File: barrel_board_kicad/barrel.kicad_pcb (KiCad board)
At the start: 2 copper layers, 29 parts, among them J1 220V, J2 12V, J3 probe/prog, J4 valve, J5 Bypass, J6 reset, K1 DIPxx-1Cxx-51x, Q1 Q_PMOS_GSD, Q2 Q_NMOS_GSD, Q3 Q_PMOS_GSD, U1 LM2576S-5, U2 ATtiny13A-SSU

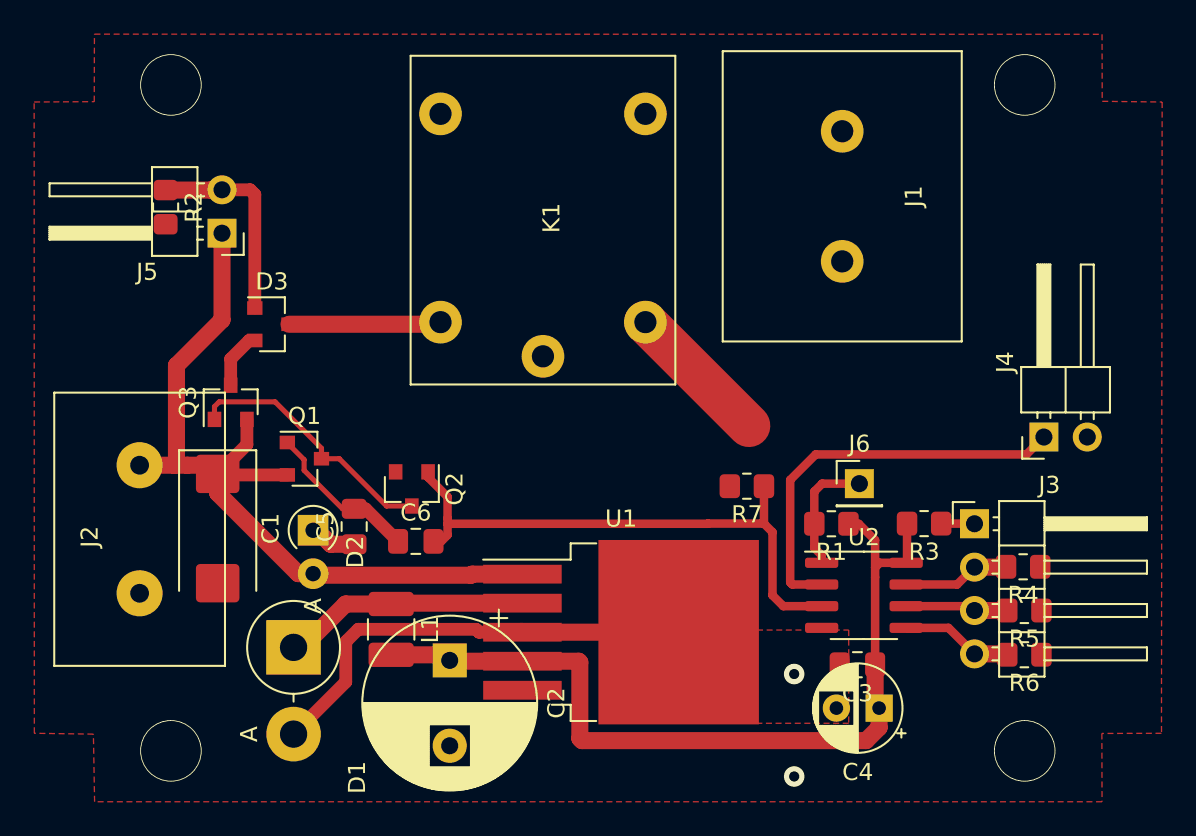
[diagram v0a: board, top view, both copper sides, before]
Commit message: Optimize the scheme
Remove redundant transistors
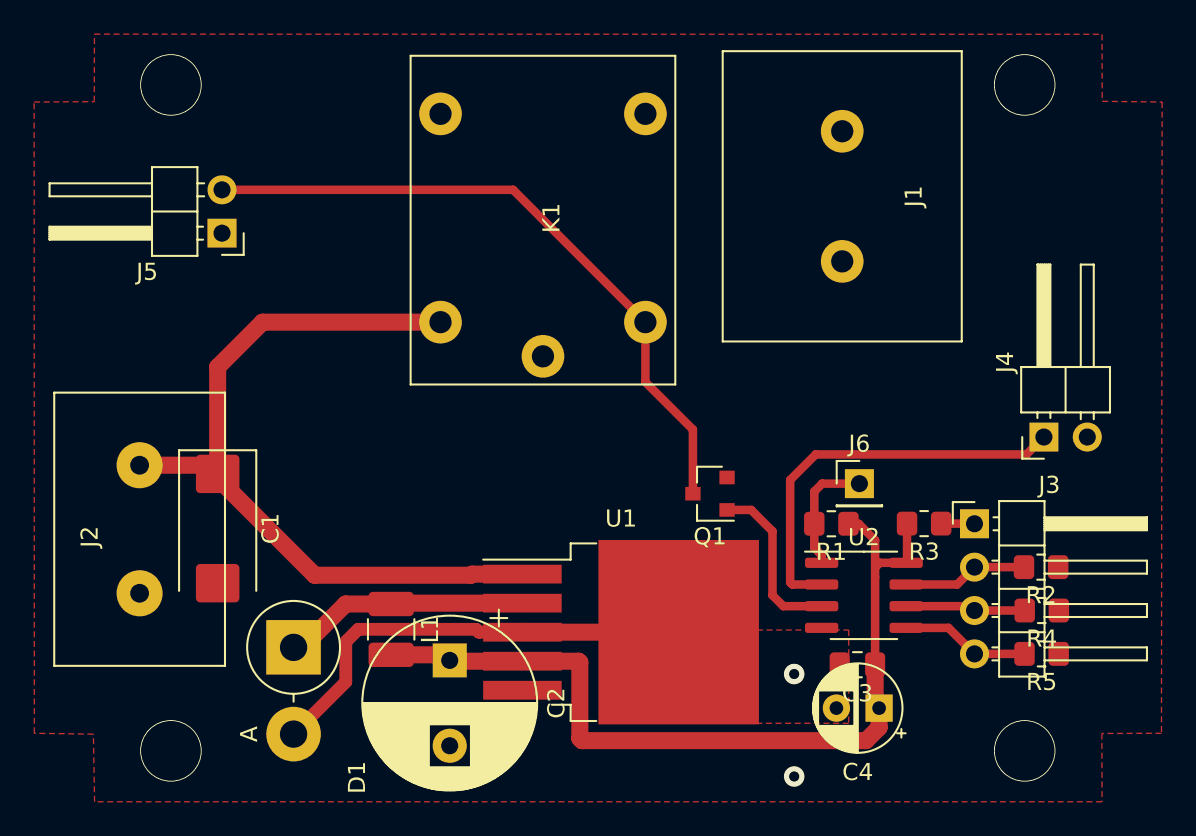
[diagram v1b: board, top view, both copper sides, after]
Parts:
- removed C5: 100nF, Capacitor_SMD:C_0805_2012Metric_Pad1.18x1.45mm_HandSolder
- removed C6: 68nF, Capacitor_SMD:C_0805_2012Metric_Pad1.18x1.45mm_HandSolder
- removed D2: D, Diode_THT:D_A-405_P2.54mm_Vertical_AnodeUp
- removed D3: BAV70, Package_TO_SOT_SMD:SOT-23
- removed Q2: Q_NMOS_GSD, Package_TO_SOT_SMD:SOT-23
- removed Q3: Q_PMOS_GSD, Package_TO_SOT_SMD:SOT-23
- removed R6, R7: 100k, Resistor_SMD:R_0805_2012Metric_Pad1.20x1.40mm_HandSolder
- Q1: value Q_PMOS_GSD -> Q_NPN_BEC
- R2, R4, R5: value 100k -> 10k
- moved R2 55.4 mm to (111.0, 78.7), turned to 180 degrees
- moved Q1 23.8 mm to (91.6, 74.4), turned to 180 degrees
- moved R4 2.78 mm to (111.0, 81.3)
- moved R5 2.73 mm to (111.0, 83.8)
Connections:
- J5 pad 1: 12v -> gnd
- J5 pad 2: Net-(D3-Pad1) -> Net-(J5-Pad2)
- K1 pad 2: gnd -> Net-(J5-Pad2)
- K1 pad 6: Net-(D3-Pad3) -> 12v
- Q1 pad 1: Net-(C5-Pad2) -> Net-(Q1-Pad1)
- Q1 pad 2: 12v -> gnd
- Q1 pad 3: Net-(Q1-Pad3) -> Net-(J5-Pad2)
- R2 pad 1: Net-(D3-Pad1) -> gnd
- R2 pad 2: gnd -> UPPER
- R4 pad 2: UPPER -> LOWER
- R5 pad 2: LOWER -> GARDEN
- U2 pad 3: Net-(C6-Pad2) -> Net-(Q1-Pad1)
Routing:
- net Net-(J5-Pad2): track 0.00 -> 39.2 mm
- net Net-(C6-Pad2): track 33.4 -> 0.00 mm
- net Net-(Q1-Pad3): track 15.3 -> 0.00 mm
- net Net-(D3-Pad1): track 12.0 -> 0.00 mm
- net Net-(Q1-Pad1): track 0.00 -> 10.1 mm
- net Net-(C5-Pad2): track 9.26 -> 0.00 mm
- net Net-(D3-Pad3): track 8.93 -> 0.00 mm
- net gnd: track 38.5 -> 29.9 mm
- net Net-(D3-Pad2): track 3.40 -> 0.00 mm
- net Net-(C5-Pad1): track 2.74 -> 0.00 mm
- net 12v: track 50.2 -> 47.6 mm
- net UPPER: track 6.28 -> 7.32 mm
- net LOWER: track 6.03 -> 7.05 mm
- net GARDEN: track 6.57 -> 7.56 mm

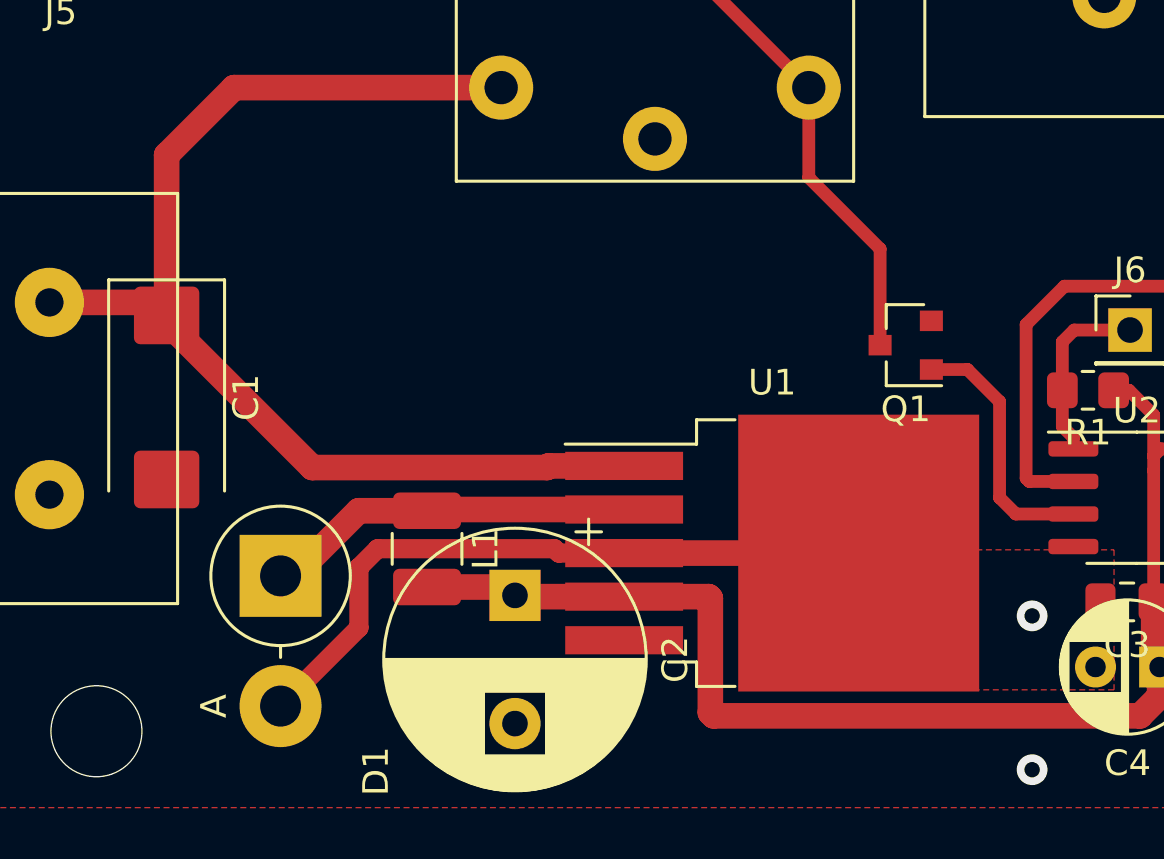
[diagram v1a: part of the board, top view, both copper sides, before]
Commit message: Fix relay scheme
Add a resistor for the transistor that controlls relay to be in a defined state at startup
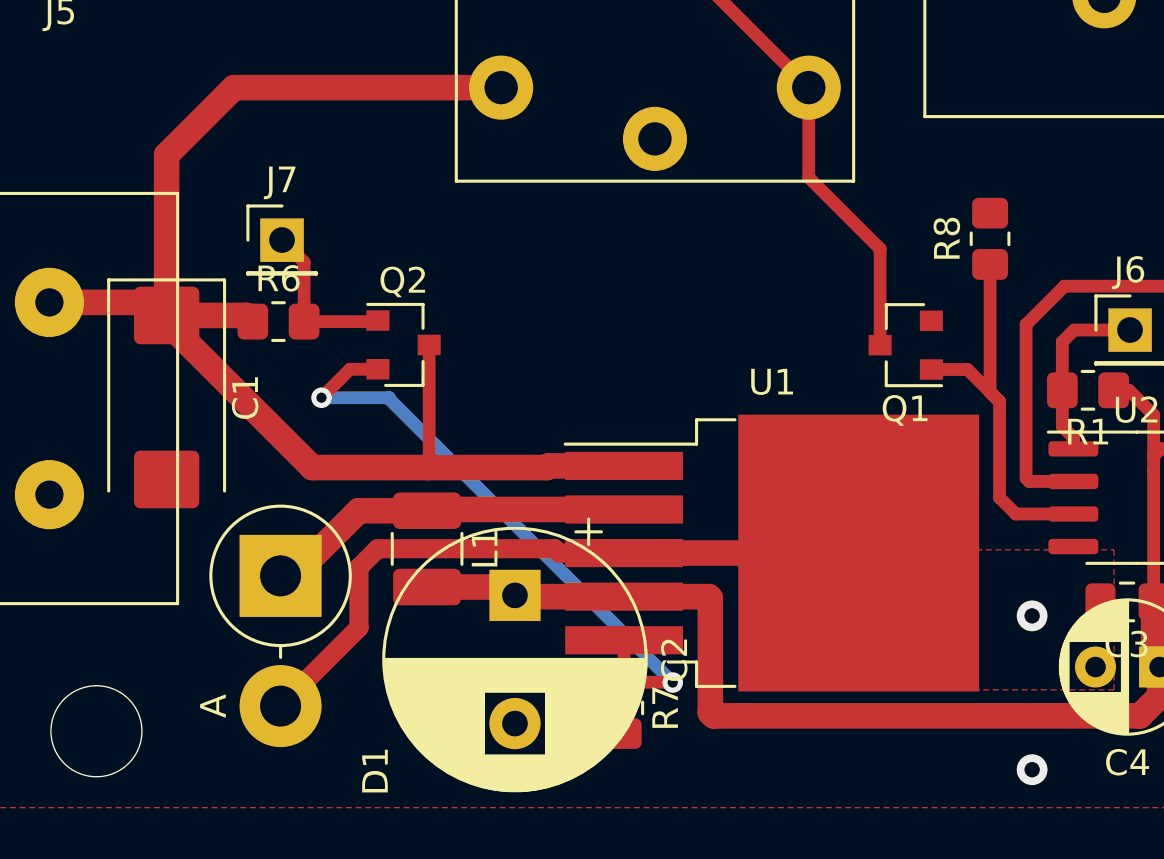
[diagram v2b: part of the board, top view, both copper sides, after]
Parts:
- added J7: emergency off, Connector_PinHeader_2.54mm:PinHeader_1x01_P2.54mm_Vertical, F.Cu at (67.2, 70.3)
- added Q2: Q_PNP_BCE, Package_TO_SOT_SMD:SOT-23, F.Cu at (72.0, 74.4)
- added R6: 10k, Resistor_SMD:R_0805_2012Metric_Pad1.20x1.40mm_HandSolder, F.Cu at (67.1, 73.5)
- added R7: 47k, Resistor_SMD:R_0805_2012Metric_Pad1.20x1.40mm_HandSolder, F.Cu at (80.6, 88.6)
- added R8: 10k, Resistor_SMD:R_0805_2012Metric_Pad1.20x1.40mm_HandSolder, F.Cu at (94.9, 70.3)
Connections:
- U1 pad 5: gnd -> Net-(Q2-Pad2)
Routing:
- net Net-(Q2-Pad2): track 0.00 -> 24.6 mm, vias 0 -> 2
- net 12v: track 47.6 -> 55.9 mm
- net Net-(J7-Pad1): track 0.00 -> 6.43 mm
- net Net-(Q1-Pad1): track 10.1 -> 15.6 mm
